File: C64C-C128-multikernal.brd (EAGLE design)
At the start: 22.5 x 41.9 mm, 15 parts, among them IC1 27C256/512, IC2 MICROCHIP_PIC12F629P

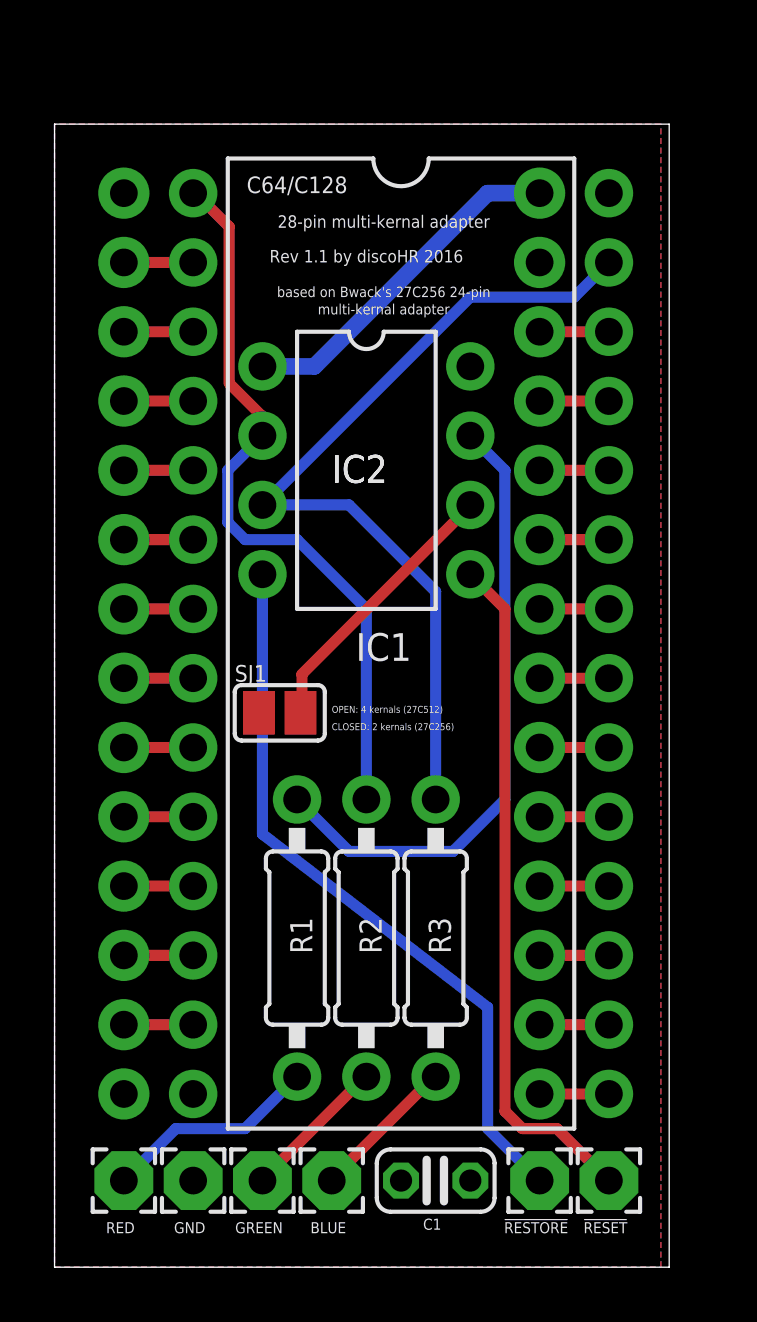
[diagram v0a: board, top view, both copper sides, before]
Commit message: expanded the pcb a bit increased the distance between EPROM and connectors increased font sizes moved some texts to the bottom added CERN OHL and GitHub URL to the silkscreen finalized rev1.1
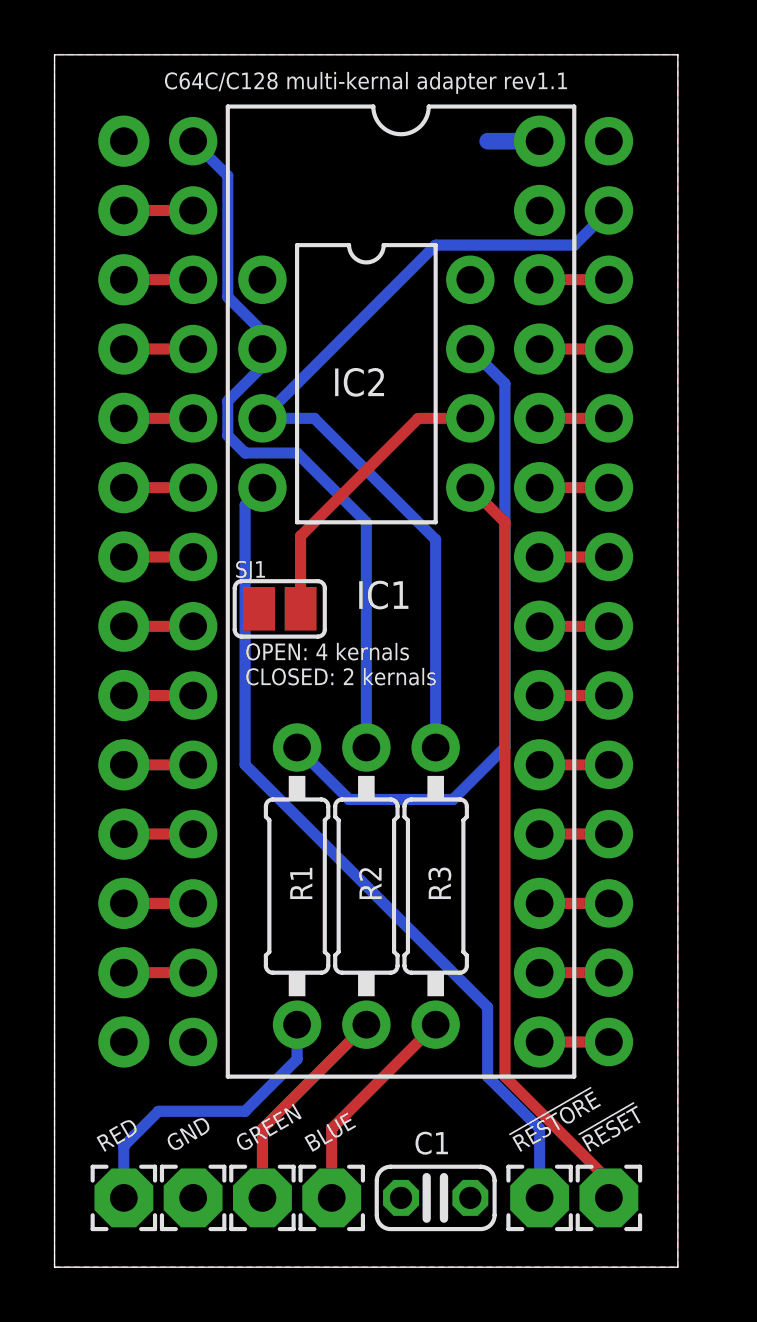
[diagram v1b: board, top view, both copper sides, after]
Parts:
- moved SJ1 3.81 mm to (8.26, 24.1)
- moved IC2 3.17 mm to (11.4, 32.4)
- moved IC1 1.91 mm to (12.7, 24.8)
- moved J1 1.91 mm to (2.54, 8.26)
- moved J2 1.91 mm to (17.8, 8.26)
- moved R1 1.91 mm to (8.89, 14.0)
- moved R2 1.91 mm to (11.4, 14.0)
- moved R3 1.91 mm to (14.0, 14.0)
- moved !RESET! 0.63 mm to (20.3, 2.54)
- moved !RESTORE! 0.63 mm to (17.8, 2.54)
- moved BLUE 0.63 mm to (10.2, 2.54)
- moved C1 0.63 mm to (14.0, 2.54)
- moved GND 0.63 mm to (5.08, 2.54)
- moved GREEN 0.63 mm to (7.62, 2.54)
- moved RED 0.63 mm to (2.54, 2.54)
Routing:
- net VCC: track 12.8 -> 1.91 mm
- net N$31: track 27.1 -> 30.8 mm
- net N$28: track 25.1 -> 28.1 mm
- net N$2: track 7.93 -> 10.8 mm
- net N$29: track 5.42 -> 7.93 mm
- net N$30: track 5.43 -> 7.93 mm
- net N$1: track 23.1 -> 24.3 mm
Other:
- board size 22.5 x 41.9 mm -> 22.8 x 44.4 mm
- board text added: "C64C/C128 multi-kernal adapter rev1.1"
- board text added: "CERN OHL 1.2 https://github.com/discoHR/C64C-C128-multikernal-adapter"
- board text added: "OPEN: 4 kernals CLOSED: 2 kernals"
- board text added: "by discoHR 2016 based on Bwack's C64 design"
- board text removed: "28-pin multi-kernal adapter"
- board text removed: "C64/C128"
- board text removed: "CLOSED: 2 kernals (27C256)"
- board text removed: "IC2"
- board text removed: "OPEN: 4 kernals (27C512)"
- board text removed: "Rev 1.1 by discoHR 2016"
- board text removed: "based on Bwack's 27C256 24-pin"
- board text removed: "multi-kernal adapter"
